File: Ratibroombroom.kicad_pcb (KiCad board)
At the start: 2 copper layers, 46 x 60 mm, 112 parts, among them J1 Conn_01x02_Male, J10 Conn_01x04_Male, J11 Conn_01x04_Male, J2 Conn_01x02_Male, J3 Conn_01x10_Male, J5 Conn_01x02_Male, J6 Conn_01x02_Male, J8 Conn_01x04_Male, J9 Conn_01x04_Male, Q1 IRLML6344, Q10 S8050, Q11 IRF7416PbF, Q2 IRLML6344, Q3 IRLML6344, Q4 IRLML6344, Q5 PT12-21B/TR8, Q6 PT12-21B/TR8, Q7 PT12-21B/TR8, Q8 PT12-21B/TR8, Q9 IRLML6344, SW1 B3U, SW2 B3U, SW3 PCM12, U1 AZ1117-3.3, U2 DRV8835, U3 AS5145B-HSST, U4 MPU-9250, U5 STM32F405RGTx, U6 AS5145B-HSST, U7 DRV8835, U8 L6932D1.2TR, U9 L6932D1.2TR, Y1 8MHZ

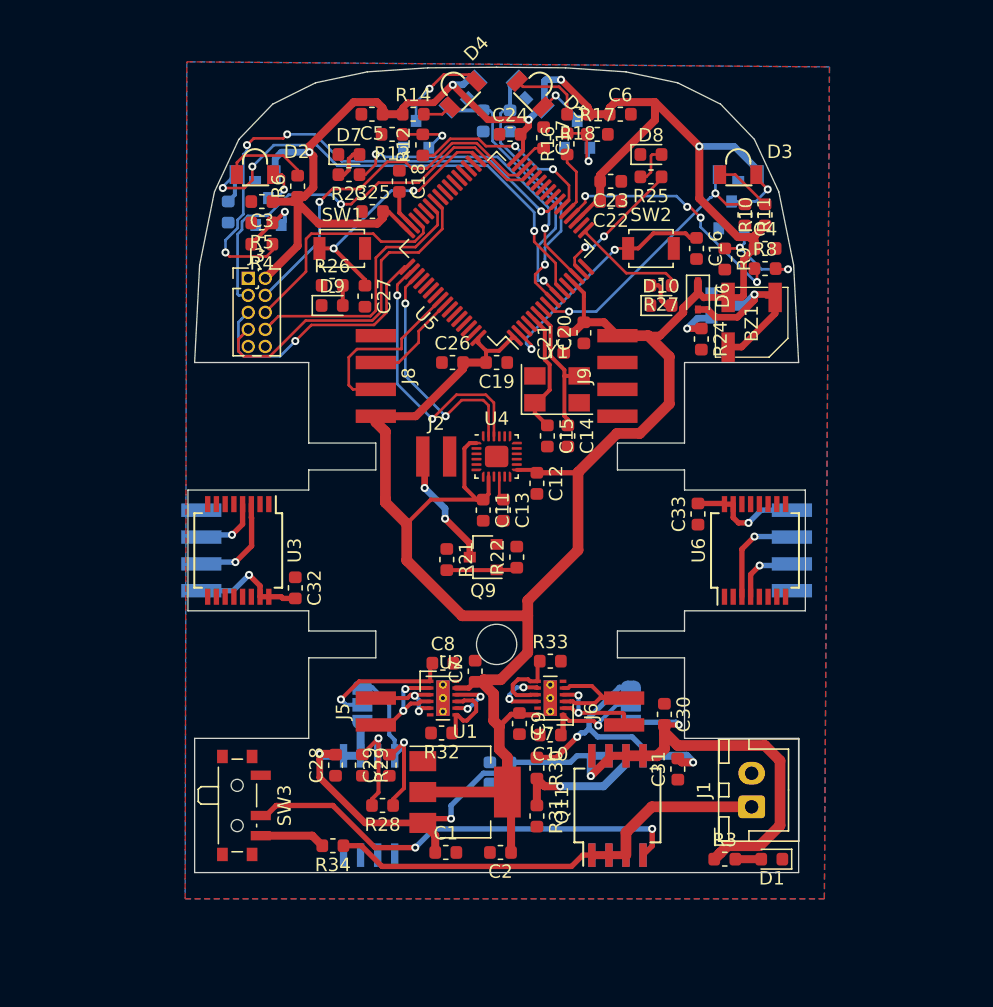
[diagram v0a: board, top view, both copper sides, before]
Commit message: More PCB routing. Add encoder magnet support boards. Include 3D models that were missing. Clean silkscreen layers. Update 3d CAD design. Include .step model of the robot.
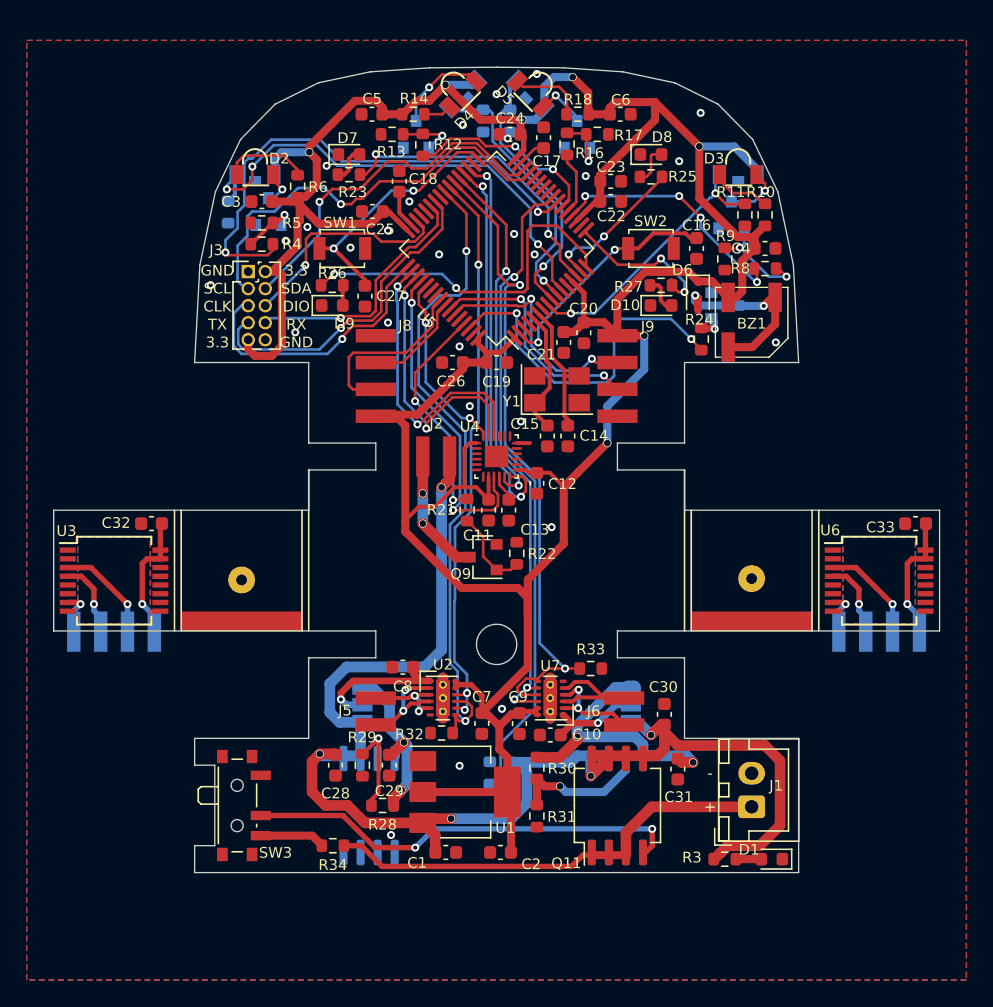
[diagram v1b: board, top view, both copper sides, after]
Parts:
- added REF**: Encoder_base_connector, Ratibroombroom:Encoder_base_connector, F.Cu at (164.0, 103.3)
- added REF**: Encoder_base_connector, Ratibroombroom:Encoder_base_connector, F.Cu at (126.0, 103.3)
- added REF**: Encoder_axle_hole, Ratibroombroom:Encoder_axle_hole, F.Cu at (126.0, 100.2)
- added REF**: Encoder_axle_hole, Ratibroombroom:Encoder_axle_hole, F.Cu at (164.0, 100.1)
- moved C33 16.2 mm to (176.2, 96.0), turned to 0 degrees
- moved C32 11.7 mm to (119.3, 96.0), turned to 0 degrees
- moved U3 9.52 mm to (116.5, 100.2), turned to 0 degrees
- moved U6 9.52 mm to (173.5, 100.2), turned to 0 degrees
- moved J10 8.88 mm to (116.5, 104.0), turned to 0 degrees
- moved J11 8.88 mm to (173.5, 104.0), turned to 0 degrees
- moved R21 3.99 mm to (142.8, 95.0)
- moved C7 3.92 mm to (143.9, 110.9), turned to 270 degrees
- moved R33 3.06 mm to (152.0, 106.8)
- moved C8 3.00 mm to (138.0, 106.7), turned to 180 degrees
- moved J3 0.50 mm to (126.5, 77.2)
- moved C11 0.40 mm to (144.4, 95.0)
- moved C13 0.40 mm to (145.9, 95.0)
- moved R22 0.29 mm to (146.5, 98.2)
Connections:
- U2 pad 13: (no net) -> GND
- U7 pad 13: (no net) -> GND
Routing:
- net /BAT_MEAS: track 1.50 -> 50.1 mm, vias 0 -> 1
- net /R_MOTOR_PWM: track 6.12 -> 51.7 mm, vias 0 -> 2
- net /L_MOTOR_PWM: track 5.66 -> 49.9 mm, vias 0 -> 2
- net /R_MOTOR_DIR: track 4.86 -> 44.9 mm, vias 2 -> 3
- net /L_MOTOR_DIR: track 4.15 -> 42.6 mm, vias 2 -> 3
- net VBUS: track 71.9 -> 105.3 mm, vias 4 -> 5
- net /IMU_INT: track 0.00 -> 29.0 mm, vias 0 -> 2
- net /IMU_FSYNC: track 0.00 -> 27.2 mm, vias 0 -> 2
- net /LED_3: track 0.00 -> 27.0 mm, vias 0 -> 2
- net /BUZZER: track 0.00 -> 26.4 mm, vias 0 -> 2
- net /IMU_MISO: track 0.00 -> 24.8 mm, vias 0 -> 2
- net GND: track 0.00 -> 18.7 mm, vias 0 -> 29
- net /R_ENCODER_B: track 0.00 -> 17.5 mm, vias 0 -> 2
- net /R_ENCODER_A: track 0.00 -> 17.4 mm, vias 0 -> 2
- net /SUCTION_PWM: track 0.00 -> 16.9 mm, vias 0 -> 2
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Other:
- board size 46 x 60 mm -> 66 x 60 mm
- board text added: "+"
- board text added: "-"
- board text added: "3.3"
- board text added: "CLK"
- board text added: "DIO"
- board text added: "GND"
- board text added: "RX"
- board text added: "SCL"
- board text added: "SDA"
- board text added: "TX"

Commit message: Change encoder board connectors so that the boards will be rotated in the final assembly. Add separate ground and power nets to encoder boards to pass DRC cleanly. Add some logos
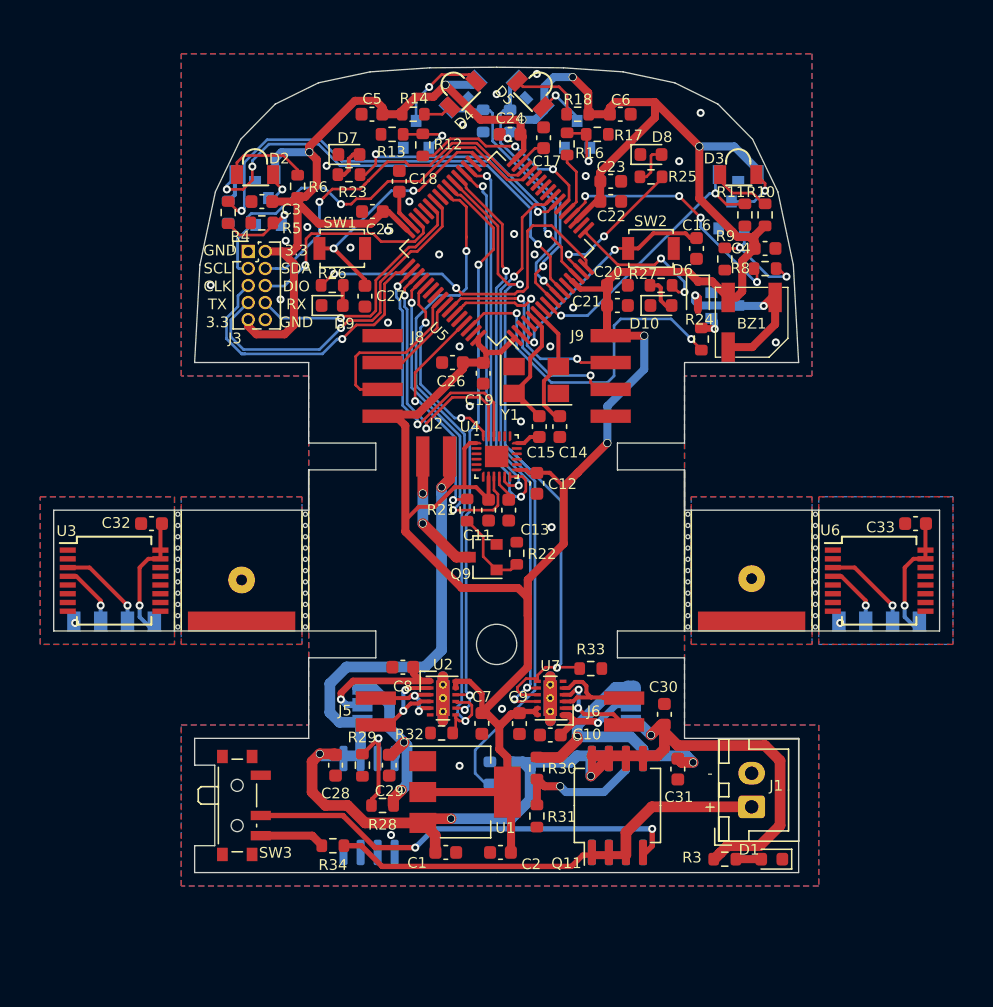
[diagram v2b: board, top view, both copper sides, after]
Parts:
- removed the REF** at (164.0, 103.3)
- removed the REF** at (126.0, 103.3)
- removed the REF** at (126.0, 100.2)
- removed the REF** at (164.0, 100.1)
- added G***: LOGO, Ratibroombroom:oshwlogo, B.Cu at (128.1, 117.0)
- added G***: LOGO, Ratibroombroom:ailogo_completo, B.Cu at (145.0, 82.8)
- added G***: LOGO, Ratibroombroom:ailogo_small, B.Cu at (173.5, 99.5)
- added G***: LOGO, Ratibroombroom:ailogo_small, B.Cu at (116.5, 99.5)
- added J12: Conn_01x01_Male, Ratibroombroom:Encoder_base_connector, F.Cu at (126.0, 103.3)
- added J13: Conn_01x01_Male, Ratibroombroom:Encoder_base_connector, F.Cu at (164.0, 103.3)
- added J4: Conn_01x01_Male, Ratibroombroom:Encoder_axle_hole, F.Cu at (126.0, 100.2)
- added J7: Conn_01x01_Male, Ratibroombroom:Encoder_axle_hole, F.Cu at (164.0, 100.1)
- added REF**: mousebites, Ratibroombroom:mousebites, F.Cu at (168.8, 95.3)
- added REF**: mousebites, Ratibroombroom:mousebites, F.Cu at (159.2, 95.3)
- added REF**: mousebites, Ratibroombroom:mousebites, F.Cu at (130.8, 95.3)
- added REF**: mousebites, Ratibroombroom:mousebites, F.Cu at (121.2, 95.3)
- J10, J11: footprint Ratibroombroom:Pad_SMD_4P_1x3mm -> Ratibroombroom:Pad_SMD_4P_1x1.5mm
- moved C21 4.85 mm to (154.0, 79.8), turned to 180 degrees
- moved C20 4.33 mm to (154.0, 78.2), turned to 180 degrees
- moved R4 3.44 mm to (125.0, 72.8), turned to 270 degrees
- moved Y1 1.70 mm to (147.9, 85.3)
- moved J3 1.50 mm to (126.5, 75.7)
- moved C19 1.28 mm to (144.0, 84.8), turned to 90 degrees
- moved C14 0.92 mm to (149.7, 88.8)
- moved C15 0.92 mm to (148.2, 88.8)
- moved J10 0.75 mm to (116.5, 103.3)
- moved J11 0.75 mm to (173.5, 103.3)
- moved J8 0.50 mm to (136.5, 85.0)
- moved J9 0.50 mm to (153.5, 85.0)
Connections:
- C32 pad 1: GND -> GND_a
- C32 pad 2: +3V3 -> +3.3V_a
- C33 pad 1: GND -> GND_b
- C33 pad 2: +3V3 -> +3.3V_b
- J10 pad 1: GND -> GND_a
- J10 pad 4: +3V3 -> +3.3V_a
- J11 pad 1: GND -> GND_b
- J11 pad 4: +3V3 -> +3.3V_b
- U3 pad 11: GND -> GND_a
- U3 pad 15: +3V3 -> +3.3V_a
- U3 pad 16: +3V3 -> +3.3V_a
- U3 pad 7: GND -> GND_a
- U6 pad 11: GND -> GND_b
- U6 pad 15: +3V3 -> +3.3V_b
- U6 pad 16: +3V3 -> +3.3V_b
- U6 pad 7: GND -> GND_b
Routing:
- net +3V3: track 272.3 -> 249.8 mm, vias 9 -> 7
- net +3.3V_a: track 0.00 -> 9.25 mm, vias 0 -> 1
- net +3.3V_b: track 0.00 -> 9.22 mm, vias 0 -> 1
- net /TX_FRONT_L: track 38.3 -> 31.7 mm
- net GND: track 18.7 -> 16.4 mm
- net /SWCLK: track 20.8 -> 22.8 mm
- net Net-(Q1-Pad1): track 4.25 -> 6.16 mm
- net /SERIAL_TX: track 24.7 -> 26.4 mm
- net /I2C_SCL: track 31.9 -> 30.2 mm
- net /OSC_OUT: track 10.3 -> 9.00 mm
- net /L_ENCODER_B: track 7.61 -> 8.62 mm
- net /SWDIO: track 17.0 -> 16.1 mm
- net /I2C_SDA: track 26.8 -> 26.0 mm
- net /RX_SIDE_R: track 20.4 -> 19.7 mm
- net /L_MOTOR_DIR: track 42.6 -> 43.3 mm
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- added copper zone on B.Cu, net GND_a
- added copper zone on F.Cu, net GND_a
- added copper zone on B.Cu, net GND_b
- added copper zone on F.Cu, net GND_b
- added copper zone on B.Cu, net GND_c
- added copper zone on F.Cu, net GND_c
- added copper zone on B.Cu, net GND_d
- added copper zone on F.Cu, net GND_d
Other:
- board text added: "https://github.com/aindustriosa/Ratibroombroom"

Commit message: Add version tag in silkscreen. Change board thickness to .8 mm
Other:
- board text added: "V0R0"

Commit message: Add BOM references
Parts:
- J12, J13: value Conn_01x01_Male -> Support board base
- J4, J7: value Conn_01x01_Male -> Support board axle
- R10, R14, R18, R6: value R -> 47R
- R11, R15, R19, R7: value R -> 20K
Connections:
- U2 pad 13: GND -> (no net)
- U7 pad 13: GND -> (no net)
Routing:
- net GND: track 16.4 -> 3.20 mm
- net (no net): track 0.00 -> 13.2 mm
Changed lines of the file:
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@@
-(kicad_pcb (version 20171130) (host pcbnew 5.1.7-a382d34a8~87~ubuntu20.04.1)
+(kicad_pcb (version 20171130) (host pcbnew "(5.1.5)-3")
   (general
     (thickness 0.8)
@@
       (psa4output false)
       (plotreference true)
-      (plotvalue true)
+      (plotvalue false)
       (plotinvisibletext false)
       (padsonsilk false)
@@
       (outputformat 1)
       (mirror false)
-      (drillshape 1)
+      (drillshape 0)
       (scaleselection 1)
-      (outputdirectory ""))
+      (outputdirectory "GERBER/"))
   )
   (net 0 "")
@@
       (effects (font (size 1 1) (thickness 0.15)))
     )
-    (fp_text value Conn_01x01_Male (at 0 -0.5) (layer F.Fab)
+    (fp_text value "Support board base" (at 0 -0.5) (layer F.Fab)
       (effects (font (size 1 1) (thickness 0.15)))
     )
@@
       (effects (font (size 1 1) (thickness 0.15)))
     )
-    (fp_text value Conn_01x01_Male (at 0 -0.5) (layer F.Fab)
+    (fp_text value "Support board base" (at 0 -0.5) (layer F.Fab)
       (effects (font (size 1 1) (thickness 0.15)))
     )
@@
       (effects (font (size 1 1) (thickness 0.15)))
     )
-    (fp_text value Conn_01x01_Male (at 0 -0.5) (layer F.Fab)
+    (fp_text value "Support board axle" (at 0 -0.5) (layer F.Fab)
       (effects (font (size 1 1) (thickness 0.15)))
     )
@@
       (effects (font (size 1 1) (thickness 0.15)))
     )
-    (fp_text value Conn_01x01_Male (at 0 -0.5) (layer F.Fab)
+    (fp_text value "Support board axle" (at 0 -0.5) (layer F.Fab)
       (effects (font (size 1 1) (thickness 0.15)))
     )
@@
       (effects (font (size 0.8 0.8) (thickness 0.15)) (justify mirror))
     )
-    (fp_text value R (at 0 -1.43 90) (layer B.Fab)
+    (fp_text value 20K (at 0 -1.43 90) (layer B.Fab)
       (effects (font (size 0.8 0.8) (thickness 0.15)) (justify mirror))
     )
@@
       (effects (font (size 0.8 0.8) (thickness 0.15)))
     )
-    (fp_text value R (at 0 1.43) (layer F.Fab)
+    (fp_text value 47R (at 0 1.43) (layer F.Fab)
       (effects (font (size 0.8 0.8) (thickness 0.15)))
     )
@@
       (effects (font (size 0.8 0.8) (thickness 0.15)) (justify mirror))
     )
-    (fp_text value R (at 0 -1.43 90) (layer B.Fab)
+    (fp_text value 20K (at 0 -1.43 90) (layer B.Fab)
       (effects (font (size 0.8 0.8) (thickness 0.15)) (justify mirror))
     )
@@
       (effects (font (size 0.8 0.8) (thickness 0.15)))
     )
-    (fp_text value R (at 0 1.43) (layer F.Fab)
+    (fp_text value 47R (at 0 1.43) (layer F.Fab)
       (effects (font (size 0.8 0.8) (thickness 0.15)))
     )
@@
       (effects (font (size 0.8 0.8) (thickness 0.15)))
     )
-    (fp_text value R (at 0 1.43 90) (layer F.Fab)
+    (fp_text value 20K (at 0 1.43 90) (layer F.Fab)
       (effects (font (size 0.8 0.8) (thickness 0.15)))
     )
@@
       (effects (font (size 0.8 0.8) (thickness 0.15)))
     )
-    (fp_text value R (at 0 1.43 90) (layer F.Fab)
+    (fp_text value 47R (at 0 1.43 90) (layer F.Fab)
       (effects (font (size 0.8 0.8) (thickness 0.15)))
     )
@@
       (effects (font (size 0.8 0.8) (thickness 0.15)) (justify mirror))
     )
-    (fp_text value R (at 0 -1.43 270) (layer B.Fab)
+    (fp_text value 20K (at 0 -1.43 270) (layer B.Fab)
       (effects (font (size 0.8 0.8) (thickness 0.15)) (justify mirror))
     )
@@
       (effects (font (size 0.8 0.8) (thickness 0.15)))
     )
-    (fp_text value R (at 0 1.43 270) (layer F.Fab)
+    (fp_text value 47R (at 0 1.43 270) (layer F.Fab)
       (effects (font (size 0.8 0.8) (thickness 0.15)))
     )
@@
     (pad "" smd rect (at 0 0.5 180) (size 0.95 0.8) (layers F.Paste))
     (pad "" smd rect (at 0 -0.5 180) (size 0.95 0.8) (layers F.Paste))
-    (pad 13 smd rect (at 0 0 180) (size 1 2.65) (layers F.Cu F.Mask)
-      (net 3 GND))
-    (pad 13 smd rect (at 0 0 180) (size 1 2.65) (layers B.Cu)
-      (net 3 GND))
-    (pad 13 thru_hole circle (at 0 1 180) (size 0.6 0.6) (drill 0.3) (layers *.Cu)
-      (net 3 GND))
-    (pad 13 thru_hole circle (at 0 -1 270) (size 0.6 0.6) (drill 0.3) (layers *.Cu)
-      (net 3 GND))
-    (pad 13 thru_hole circle (at 0 0 180) (size 0.6 0.6) (drill 0.3) (layers *.Cu)
-      (net 3 GND))
+    (pad 13 smd rect (at 0 0 180) (size 1 2.65) (layers F.Cu F.Mask))
+    (pad 13 smd rect (at 0 0 180) (size 1 2.65) (layers B.Cu))
+    (pad 13 thru_hole circle (at 0 1 180) (size 0.6 0.6) (drill 0.3) (layers *.Cu))
+    (pad 13 thru_hole circle (at 0 -1 270) (size 0.6 0.6) (drill 0.3) (layers *.Cu))
+    (pad 13 thru_hole circle (at 0 0 180) (size 0.6 0.6) (drill 0.3) (layers *.Cu))
     (pad 12 smd rect (at 0.95 -1.25 180) (size 0.5 0.25) (layers F.Cu F.Paste F.Mask)
       (net 2 +3V3))
@@
     (pad "" smd rect (at 0 0.5) (size 0.95 0.8) (layers F.Paste))
     (pad "" smd rect (at 0 -0.5) (size 0.95 0.8) (layers F.Paste))
-    (pad 13 smd rect (at 0 0) (size 1 2.65) (layers F.Cu F.Mask)
-      (net 3 GND))
-    (pad 13 smd rect (at 0 0) (size 1 2.65) (layers B.Cu)
-      (net 3 GND))
-    (pad 13 thru_hole circle (at 0 1) (size 0.6 0.6) (drill 0.3) (layers *.Cu)
-      (net 3 GND))
-    (pad 13 thru_hole circle (at 0 -1 90) (size 0.6 0.6) (drill 0.3) (layers *.Cu)
-      (net 3 GND))
-    (pad 13 thru_hole circle (at 0 0) (size 0.6 0.6) (drill 0.3) (layers *.Cu)
-      (net 3 GND))
+    (pad 13 smd rect (at 0 0) (size 1 2.65) (layers F.Cu F.Mask))
+    (pad 13 smd rect (at 0 0) (size 1 2.65) (layers B.Cu))
+    (pad 13 thru_hole circle (at 0 1) (size 0.6 0.6) (drill 0.3) (layers *.Cu))
+    (pad 13 thru_hole circle (at 0 -1 90) (size 0.6 0.6) (drill 0.3) (layers *.Cu))
+    (pad 13 thru_hole circle (at 0 0) (size 0.6 0.6) (drill 0.3) (layers *.Cu))
     (pad 12 smd rect (at 0.95 -1.25) (size 0.5 0.25) (layers F.Cu F.Paste F.Mask)
       (net 2 +3V3))
@@
   (via (at 160.2 65.4) (size 0.6) (drill 0.3) (layers F.Cu B.Cu) (net 3))
   (via (at 158.6 69) (size 0.6) (drill 0.3) (layers F.Cu B.Cu) (net 3))
-  (segment (start 149 110.7) (end 149 107.4) (width 0.8) (layer F.Cu) (net 3))
+  (segment (start 149 110.7) (end 149 107.4) (width 0.8) (layer F.Cu) (net 0))
   (via (at 145.4 109.8) (size 0.6) (drill 0.3) (layers F.Cu B.Cu) (net 3))
   (via (at 165.8 82.5) (size 0.6) (drill 0.3) (layers F.Cu B.Cu) (net 3))
@@
   (via (at 138.5 72) (size 0.6) (drill 0.3) (layers F.Cu B.Cu) (net 3))
   (via (at 150.7 79.9) (size 0.6) (drill 0.3) (layers F.Cu B.Cu) (net 3))
-  (segment (start 149 107.4) (end 149 110.7) (width 0.8) (layer B.Cu) (net 3))
-  (segment (start 141 107.4) (end 141 110.7) (width 0.8) (layer B.Cu) (net 3))
-  (segment (start 141 110.7) (end 141 107.4) (width 0.8) (layer F.Cu) (net 3))
+  (segment (start 149 107.4) (end 149 110.7) (width 0.8) (layer B.Cu) (net 0))
+  (segment (start 141 107.4) (end 141 110.7) (width 0.8) (layer B.Cu) (net 0))
+  (segment (start 141 110.7) (end 141 107.4) (width 0.8) (layer F.Cu) (net 0))
   (via (at 128.9 79.3) (size 0.6) (drill 0.3) (layers F.Cu B.Cu) (net 3))
   (via (at 149 82.8) (size 0.6) (drill 0.3) (layers F.Cu B.Cu) (net 3))

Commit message: Change R24 value to 1k8 to increase buzzer loudness
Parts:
- R24: value 10k -> 1.8k
